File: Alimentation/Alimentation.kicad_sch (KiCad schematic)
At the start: 18 parts, among them J1 connector_battery, J2 connector_battery, J3 RJ_can, J4 USB_A, J5 Conn_01x02_Male, J7 Conn_01x02_Male, U1 JCK2012S12, U2 JCK2012S05

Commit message: Ajout de la led
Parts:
- added D3: (no value), symbol Device:LED
- added R4: (no value), symbol Device:R
- J6: value (none) -> Conn_01x03_Male; footprint (none) -> Connector_PinHeader_2.54mm:PinHeader_1x03_P2.54mm_Horizontal
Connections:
- net GND: now also D3.1 (K)
- net V_batt: now also R4.1
- new net: D3.2 (A), R4.2
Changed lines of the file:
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@@
   (no_connect (at 185.42 36.83))
   (no_connect (at 104.14 106.045))
+  (wire (pts (xy 55.88 46.99) (xy 55.88 44.45))
+    (stroke (width 0) (type default) (color 0 0 0 0))
+  )
   (wire (pts (xy 88.9 33.02) (xy 93.98 33.02))
     (stroke (width 0) (type default) (color 0 0 0 0))
@@
     (stroke (width 0) (type default) (color 0 0 0 0))
   )
+  (wire (pts (xy 30.48 44.45) (xy 34.29 44.45))
+    (stroke (width 0) (type default) (color 0 0 0 0))
+  )
   (wire (pts (xy 93.98 71.12) (xy 96.52 71.12))
     (stroke (width 0) (type default) (color 0 0 0 0))
@@
     (stroke (width 0) (type default) (color 0 0 0 0))
   )
-  (polyline (pts (xy 15.24 15.24) (xy 15.24 40.64))
-    (stroke (width 0) (type default) (color 0 0 0 0))
-  )
-  (wire (pts (xy 49.53 26.67) (xy 48.26 26.67))
+  (polyline (pts (xy 15.24 15.24) (xy 15.24 54.61))
+    (stroke (width 0) (type default) (color 0 0 0 0))
+  )
+  (wire (pts (xy 55.88 26.67) (xy 48.26 26.67))
     (stroke (width 0) (type default) (color 0 0 0 0))
   )
@@
     (stroke (width 0) (type default) (color 0 0 0 0))
   )
+  (wire (pts (xy 41.91 44.45) (xy 45.72 44.45))
+    (stroke (width 0) (type default) (color 0 0 0 0))
+  )
+  (wire (pts (xy 55.88 44.45) (xy 53.34 44.45))
+    (stroke (width 0) (type default) (color 0 0 0 0))
+  )
   (polyline (pts (xy 69.85 123.19) (xy 195.58 123.19))
     (stroke (width 0) (type default) (color 0 0 0 0))
@@
     (stroke (width 0) (type default) (color 0 0 0 0))
   )
-  (polyline (pts (xy 66.04 40.64) (xy 66.04 15.24))
+  (polyline (pts (xy 66.04 54.61) (xy 66.04 15.24))
     (stroke (width 0) (type default) (color 0 0 0 0))
   )
@@
     (stroke (width 0) (type default) (color 0 0 0 0))
   )
-  (polyline (pts (xy 15.24 40.64) (xy 66.04 40.64))
+  (polyline (pts (xy 15.24 54.61) (xy 66.04 54.61))
     (stroke (width 0) (type default) (color 0 0 0 0))
   )
@@
     )
   )
-  (global_label "V_batt" (shape input) (at 49.53 26.67 0) (fields_autoplaced)
+  (global_label "V_batt" (shape input) (at 30.48 44.45 180) (fields_autoplaced)
+    (effects (font (size 1.27 1.27)) (justify right))
+    (property "Références Inter-Feuilles" "${INTERSHEET_REFS}" (id 0) (at 22.2612 44.3706 0)
+      (effects (font (size 1.27 1.27)) (justify right) hide)
+    )
+  )
+  (global_label "V_batt" (shape input) (at 55.88 26.67 0) (fields_autoplaced)
     (effects (font (size 1.27 1.27)) (justify left))
-    (property "Referencias entre hojas" "${INTERSHEET_REFS}" (id 0) (at 57.7488 26.5906 0)
+    (property "Referencias entre hojas" "${INTERSHEET_REFS}" (id 0) (at 64.0988 26.5906 0)
       (effects (font (size 1.27 1.27)) (justify left) hide)
     )
@@
       (effects (font (size 1.27 1.27)) (justify right))
     )
-    (property "Value" "" (id 1) (at 157.48 64.7701 0)
-      (effects (font (size 1.27 1.27)) (justify right))
-    )
-    (property "Footprint" "" (id 2) (at 158.75 66.04 0)
+    (property "Value" "Conn_01x03_Male" (id 1) (at 157.48 64.7701 0)
+      (effects (font (size 1.27 1.27)) (justify right))
+    )
+    (property "Footprint" "Connector_PinHeader_2.54mm:PinHeader_1x03_P2.54mm_Horizontal" (id 2) (at 158.75 66.04 0)
       (effects (font (size 1.27 1.27)) hide)
     )
@@
     (pin "1")
   )
+  (symbol (lib_id "power:GND") (at 55.88 46.99 0) (unit 1)
+    (in_bom yes) (on_board yes) (fields_autoplaced)
+    (property "Reference" "#PWR08" (id 0) (at 55.88 53.34 0)
+      (effects (font (size 1.27 1.27)) hide)
+    )
+    (property "Value" "" (id 1) (at 55.88 52.07 0))
+    (property "Footprint" "" (id 2) (at 55.88 46.99 0)
+      (effects (font (size 1.27 1.27)) hide)
+    )
+    (property "Datasheet" "" (id 3) (at 55.88 46.99 0)
+      (effects (font (size 1.27 1.27)) hide)
+    )
+    (pin "1")
+  )
   (symbol (lib_id "Device:LED") (at 138.43 105.41 90) (unit 1)
     (in_bom yes) (on_board yes) (fields_autoplaced)
@@
     )
     (pin "1")
+  )
+  (symbol (lib_id "Device:LED") (at 49.53 44.45 180) (unit 1)
+    (in_bom yes) (on_board yes) (fields_autoplaced)
+    (property "Reference" "D3" (id 0) (at 51.1175 36.83 0))
+    (property "Value" "" (id 1) (at 51.1175 39.37 0))
+    (property "Footprint" "" (id 2) (at 49.53 44.45 0)
+      (effects (font (size 1.27 1.27)) hide)
+    )
+    (property "Datasheet" "~" (id 3) (at 49.53 44.45 0)
+      (effects (font (size 1.27 1.27)) hide)
+    )
+    (pin "1")
+    (pin "2")
   )
   (symbol (lib_id "power:GND") (at 185.42 31.75 90) (unit 1)
@@
     (pin "2")
   )
+  (symbol (lib_id "Device:R") (at 38.1 44.45 90) (unit 1)
+    (in_bom yes) (on_board yes) (fields_autoplaced)
+    (property "Reference" "R4" (id 0) (at 38.1 38.1 90))
+    (property "Value" "" (id 1) (at 38.1 40.64 90))
+    (property "Footprint" "" (id 2) (at 38.1 46.228 90)
+      (effects (font (size 1.27 1.27)) hide)
+    )
+    (property "Datasheet" "~" (id 3) (at 38.1 44.45 0)
+      (effects (font (size 1.27 1.27)) hide)
+    )
+    (pin "1")
+    (pin "2")
+  )
   (symbol (lib_id "Connector:Conn_01x02_Male") (at 161.29 110.49 0) (unit 1)
     (in_bom yes) (on_board yes) (fields_autoplaced)
@@
       (reference "#PWR07") (unit 1) (value "GND") (footprint "")
     )
+    (path "/991d7762-0dc1-43bc-8d9f-6514811c7b78"
+      (reference "#PWR08") (unit 1) (value "GND") (footprint "")
+    )
     (path "/fc53dd7e-a77a-4253-91fc-d4db2261d8bc"
       (reference "#PWR0101") (unit 1) (value "GND") (footprint "")
@@
       (reference "D2") (unit 1) (value "LED") (footprint "LED_THT:LED_D5.0mm")
     )
+    (path "/a84fb60b-103b-4fd2-825d-e10a02cf3329"
+      (reference "D3") (unit 1) (value "LED") (footprint "LED_THT:LED_D5.0mm")
+    )
     (path "/56b4d4d4-4eb2-4c73-b8a0-6cebc34be760"
       (reference "J1") (unit 1) (value "connector_battery") (footprint "Robot:WR_TBL_3137_2pins")
@@
       (reference "R3") (unit 1) (value "120") (footprint "Resistor_SMD:R_0805_2012Metric_Pad1.20x1.40mm_HandSolder")
     )
+    (path "/e0f0e473-7e5f-4b37-9b31-d09320a17856"
+      (reference "R4") (unit 1) (value "1500") (footprint "Resistor_SMD:R_0805_2012Metric_Pad1.20x1.40mm_HandSolder")
+    )
     (path "/23ca2ac7-14de-4e83-9737-7f6217f4b3ef"

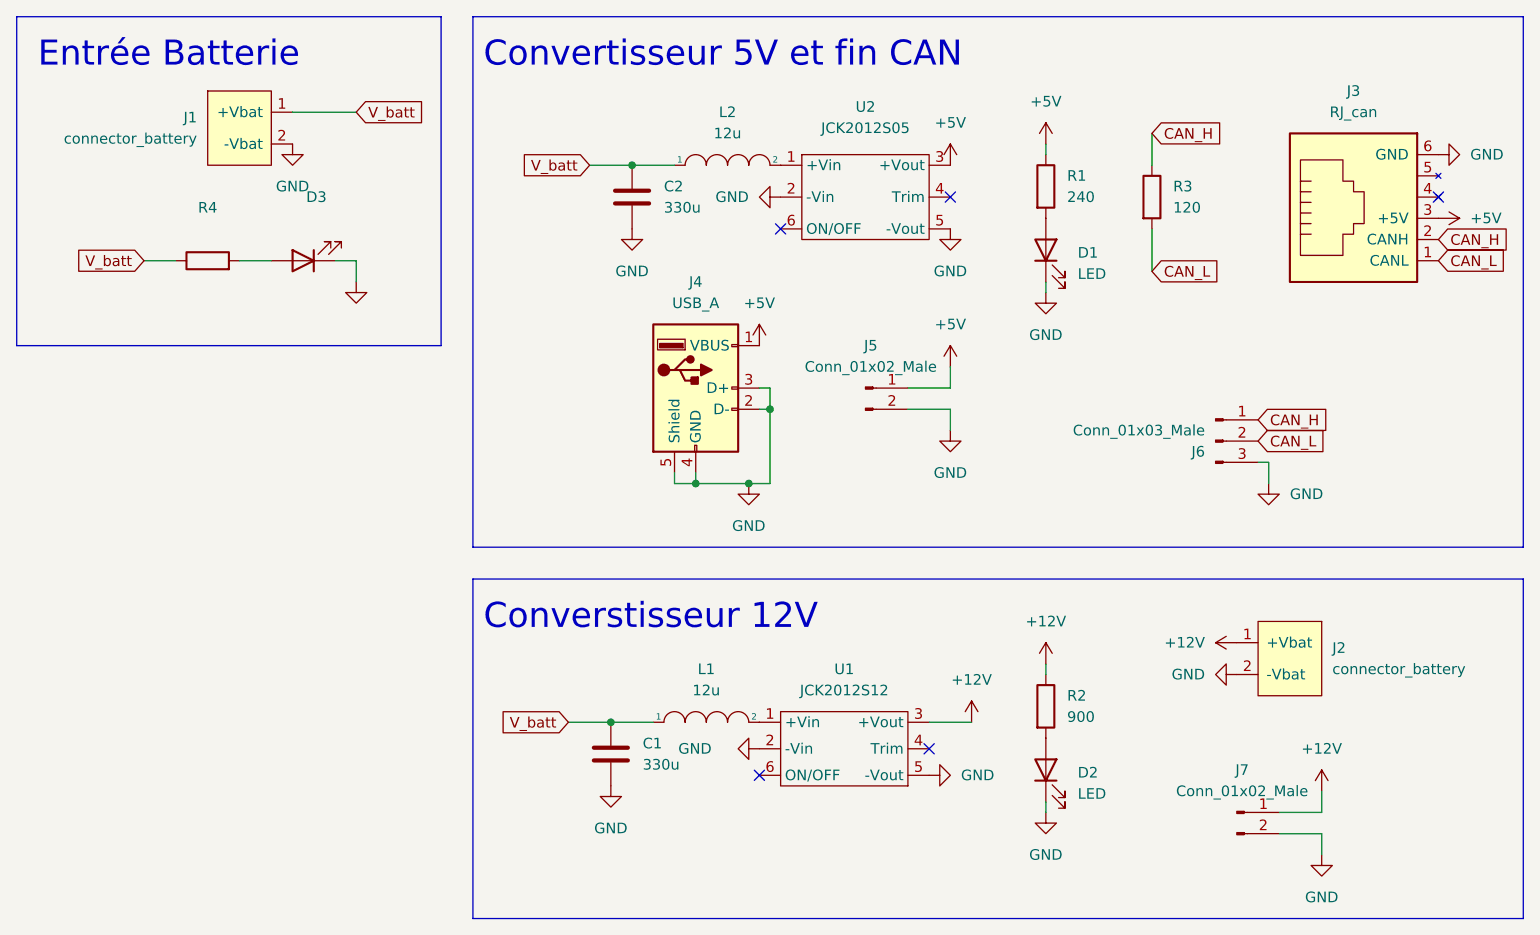
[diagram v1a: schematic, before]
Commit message: Update alimentation; Add Base roulante
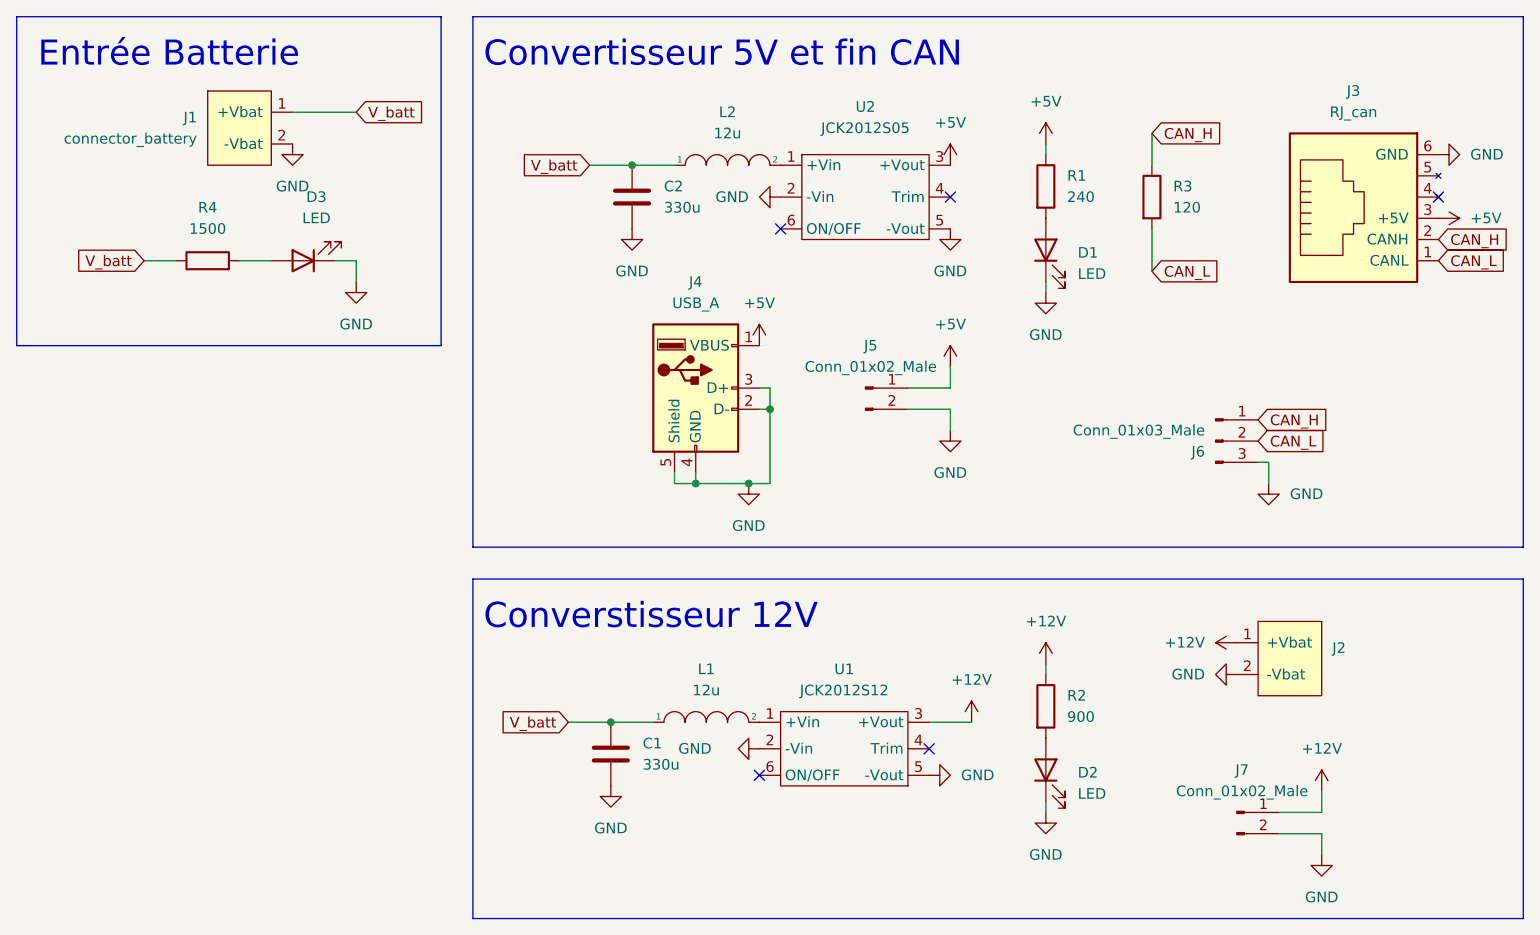
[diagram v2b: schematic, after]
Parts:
- D3: value (none) -> LED; footprint (none) -> LED_THT:LED_D5.0mm
- J2: value connector_battery -> (none)
- R4: value (none) -> 1500; footprint (none) -> Resistor_SMD:R_0805_2012Metric_Pad1.20x1.40mm_HandSolder
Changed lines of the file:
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@@
       (effects (font (size 1.27 1.27)) hide)
     )
-    (property "Value" "" (id 1) (at 55.88 52.07 0))
+    (property "Value" "GND" (id 1) (at 55.88 52.07 0))
     (property "Footprint" "" (id 2) (at 55.88 46.99 0)
       (effects (font (size 1.27 1.27)) hide)
@@
     (in_bom yes) (on_board yes) (fields_autoplaced)
     (property "Reference" "D3" (id 0) (at 51.1175 36.83 0))
-    (property "Value" "" (id 1) (at 51.1175 39.37 0))
-    (property "Footprint" "" (id 2) (at 49.53 44.45 0)
+    (property "Value" "LED" (id 1) (at 51.1175 39.37 0))
+    (property "Footprint" "LED_THT:LED_D5.0mm" (id 2) (at 49.53 44.45 0)
       (effects (font (size 1.27 1.27)) hide)
     )
@@
     (in_bom yes) (on_board yes) (fields_autoplaced)
     (property "Reference" "R4" (id 0) (at 38.1 38.1 90))
-    (property "Value" "" (id 1) (at 38.1 40.64 90))
-    (property "Footprint" "" (id 2) (at 38.1 46.228 90)
+    (property "Value" "1500" (id 1) (at 38.1 40.64 90))
+    (property "Footprint" "Resistor_SMD:R_0805_2012Metric_Pad1.20x1.40mm_HandSolder" (id 2) (at 38.1 46.228 90)
       (effects (font (size 1.27 1.27)) hide)
     )
@@
       (effects (font (size 1.27 1.27)) (justify right))
     )
-    (property "Value" "connector_battery" (id 1) (at 172.72 93.3449 0)
+    (property "Value" "" (id 1) (at 172.72 93.3449 0)
       (effects (font (size 1.27 1.27)) (justify right))
     )
@@
     )
     (path "/fa39d8ee-6dae-4e54-bd6f-0b3b99507798"
-      (reference "J2") (unit 1) (value "connector_battery") (footprint "Robot:WR_TBL_3137_2pins")
+      (reference "J2") (unit 1) (value "connector_power") (footprint "Robot:WR_TBL_3137_2pins")
     )
     (path "/0e08dcd6-2150-4984-bad1-952c00479f53"
